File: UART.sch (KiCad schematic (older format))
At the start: 15 parts, among them J3 Grove, J4 Conn_02x04_Odd_Even, SW1 SW_Push, SW2 SW_Push, U7 ESP-12E, X1 XBee_S3

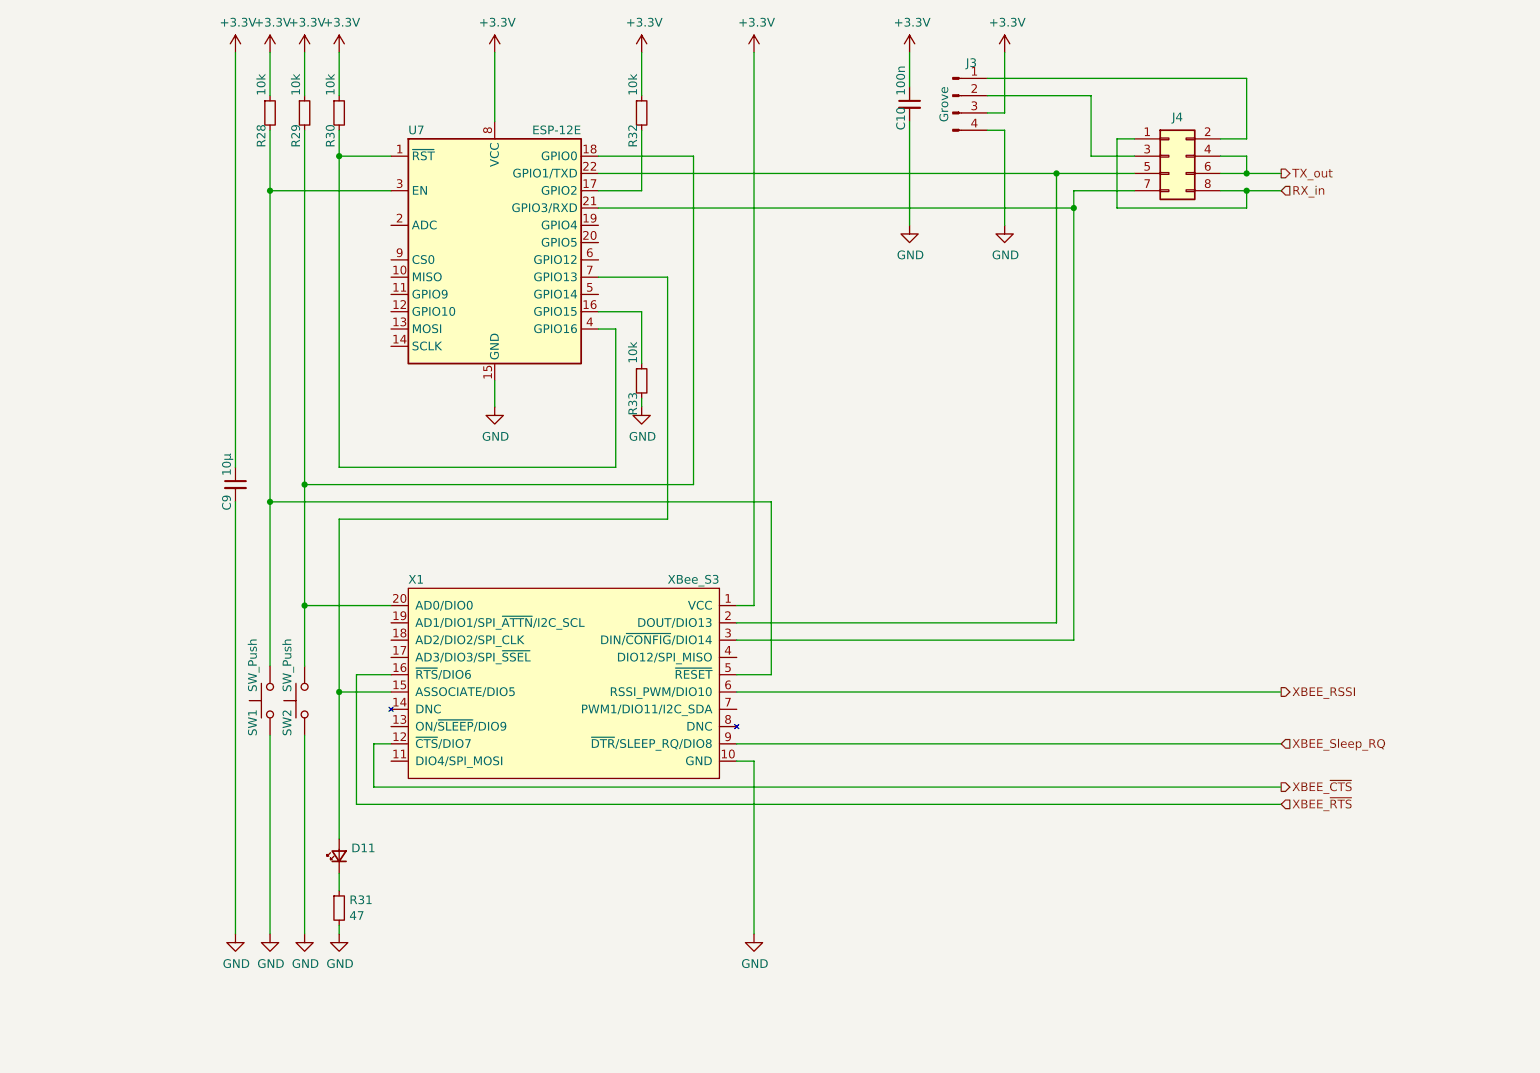
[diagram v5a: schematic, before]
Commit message: Switched ESP8266F to MICRO32
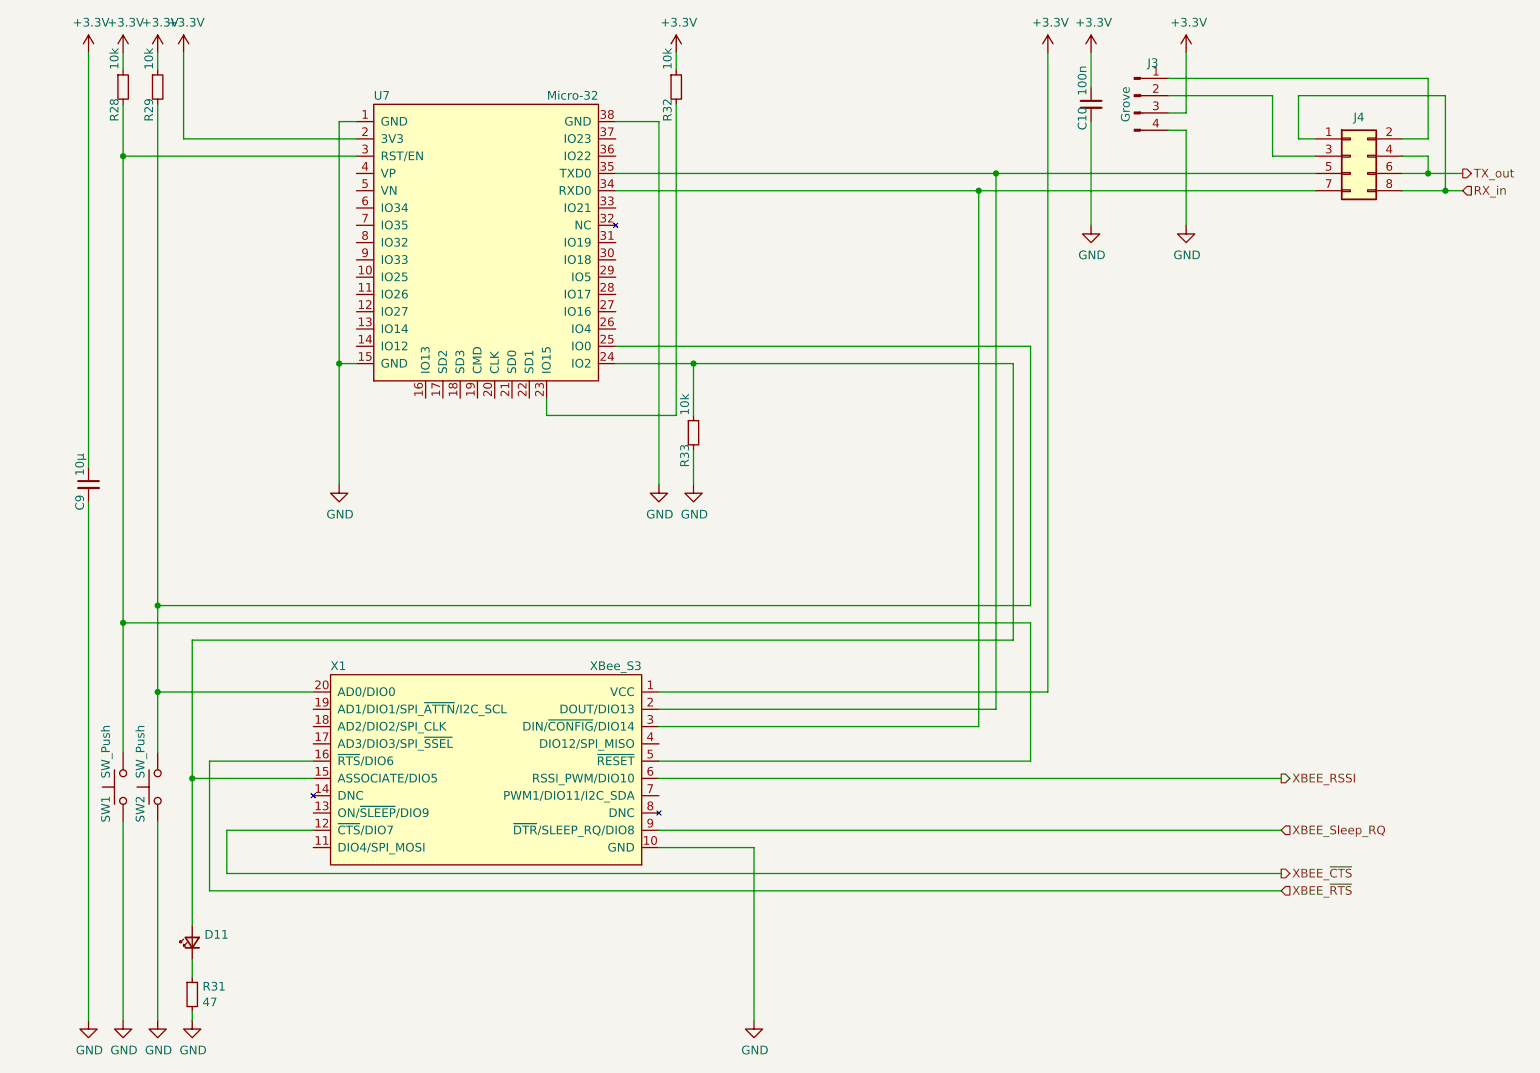
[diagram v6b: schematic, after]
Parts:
- removed R30: 10k, Resistor_SMD:R_0603_1608Metric_Pad1.05x0.95mm_HandSolder, symbol MCT_Labor_5529-rescue:R_Small-Device
- removed U7: ESP-12E, RF_Module:ESP-12E, symbol MCT_Labor_5529-rescue:ESP-12E-RF_Module
- added U7: Micro-32, HS-Wismar:micro32, symbol HS-Wismar:Micro-32
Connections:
- net +3V3: now also U7.2 (3V3)
- net GND: now also U7.1 (GND), U7.15 (GND), U7.38 (GND)
- net at R33.1: now also D11.2 (A), X1.15 (ASSOCIATE/DIO5), U7.24 (IO2)
- net at R32.2: now also U7.23 (IO15)
- net at R29.2, SW2.2, X1.20 (AD0/DIO0): now also U7.25 (IO0)
- net at J4.7 (Pin_7), X1.3 (DIN/~CONFIG~/DIO14): now also U7.34 (RXD0)
- net at J4.5 (Pin_5), X1.2 (DOUT/DIO13): now also U7.35 (TXD0)
- net at R28.2, SW1.2, X1.5 (~RESET): now also U7.3 (RST/EN)
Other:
- moved on the sheet: C10, C9, D11, J3, J4, R28, R29, R31, R32, R33, SW1, SW2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
